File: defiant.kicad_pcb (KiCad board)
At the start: 2 copper layers, 126.6 x 99.2 mm, 55 parts, among them J1 Conn_01x02_Pin, SW1 SW_Push, SW2 SW_Push, SW3 SW_DP3T, T0 SW_PUSH, T1 SW_PUSH, T2 SW_PUSH, T3 SW_PUSH, T4 SW_PUSH, U1 Seeed Studio XIAO BLE

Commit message: Update production files
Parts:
- moved SW3 0.25 mm to (201.3, 93.6)
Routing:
- net Net-(J1-Pin_1): track 52.7 -> 34.8 mm
- net col3: track 151.6 -> 148.3 mm
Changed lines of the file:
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@@
         (effects (font (size 0.6096 0.6096) (thickness 0.0762)) (justify mirror))
     )
-    (fp_text user "XIAO" (at 0 6.5 -90 unlocked) (layer "F.SilkS")
+    (fp_text user "Seeed Studio" (at 0 4.5 -90 unlocked) (layer "F.SilkS")
         (effects (font (size 1 1) (thickness 0.15)))
     )
-    (fp_text user "Seeed Studio" (at 0 4.5 -90 unlocked) (layer "F.SilkS")
+    (fp_text user "XIAO" (at 0 6.5 -90 unlocked) (layer "F.SilkS")
         (effects (font (size 1 1) (thickness 0.15)))
     )
@@
     (pad "11" smd rect (at 9.25 0 270) (size 3 2) (layers "B.Cu" "B.Paste" "B.Mask")
       (net 24 "row3") (pinfunction "PA6_A10_D10_MOSI") (pintype "unspecified"))
+    (pad "17" thru_hole circle (at -1.27 -8.39) (size 2.2 2.2) (drill 1.5) (layers "*.Cu" "*.Mask"))
+    (pad "18" thru_hole circle (at 1.27 -8.39) (size 2.2 2.2) (drill 1.5) (layers "*.Cu" "*.Mask"))
     (pad "19" thru_hole circle (at -1.27 -5.85) (size 2.2 2.2) (drill 1.5) (layers "*.Cu" "*.Mask")
       (net 35 "Net-(U1-RESET)") (pinfunction "RESET") (pintype "input"))
@@
   )
   (footprint "Button_Switch_THT:SW_CuK_JS202011AQN_DPDT_Angled" (layer "B.Cu")
-    (at 201.277964 93.85677 -90)
+    (at 201.27 93.61 -90)
     (descr "CuK sub miniature slide switch, JS series, DPDT, right angle, http://www.ckswitches.com/media/1422/js.pdf")
     (tags "switch DPDT")
@@
   (via (at 119.176007 98.57) (size 0.8) (drill 0.4) (layers "F.Cu" "B.Cu") (net 12))
   (segment (start 119.117785 100.857218) (end 119.117785 98.628222) (width 0.4) (layer "B.Cu") (net 12))
+  (segment (start 199.02 114.285891) (end 199.02 109.205505) (width 0.4) (layer "F.Cu") (net 13))
   (segment (start 163.265036 129.579225) (end 163.886009 127.961535) (width 0.4) (layer "F.Cu") (net 13))
   (segment (start 161.573594 128.929942) (end 163.265036 129.579225) (width 0.4) (layer "F.Cu") (net 13))
   (segment (start 154.24 64.88) (end 154.24 67.047218) (width 0.4) (layer "F.Cu") (net 13))
-  (segment (start 202.424109 117.69) (end 203.87 116.244109) (width 0.4) (layer "F.Cu") (net 13))
   (segment (start 154.22 83.45) (end 154.22 85.617218) (width 0.4) (layer "F.Cu") (net 13))
-  (segment (start 200.32 117.69) (end 202.424109 117.69) (width 0.4) (layer "F.Cu") (net 13))
-  (segment (start 203.87 107.416079) (end 200.100411 103.64649) (width 0.4) (layer "F.Cu") (net 13))
+  (segment (start 200.31 117.68) (end 200.31 115.575891) (width 0.4) (layer "F.Cu") (net 13))
+  (segment (start 200.100411 108.125094) (end 200.100412 102.905094) (width 0.4) (layer "F.Cu") (net 13))
+  (segment (start 200.32 117.69) (end 200.31 117.68) (width 0.4) (layer "F.Cu") (net 13))
+  (segment (start 199.02 109.205505) (end 200.100411 108.125094) (width 0.4) (layer "F.Cu") (net 13))
   (segment (start 154.12 103.11) (end 154.12 105.277218) (width 0.4) (layer "F.Cu") (net 13))
-  (segment (start 200.100411 103.64649) (end 200.100412 102.905094) (width 0.4) (layer "F.Cu") (net 13))
-  (segment (start 203.87 116.244109) (end 203.87 107.416079) (width 0.4) (layer "F.Cu") (net 13))
+  (segment (start 200.31 115.575891) (end 199.02 114.285891) (width 0.4) (layer "F.Cu") (net 13))
   (via (at 161.573594 128.929942) (size 0.8) (drill 0.4) (layers "F.Cu" "B.Cu") (net 13))
   (via (at 154.12 103.11) (size 0.8) (drill 0.4) (layers "F.Cu" "B.Cu") (net 13))
@@
   (segment (start 173.17 103) (end 173.17 105.167218) (width 0.4) (layer "F.Cu") (net 17))
   (segment (start 184.23 109.59) (end 173.277964 109.59) (width 0.4) (layer "F.Cu") (net 17))
-  (segment (start 202.69 118.91) (end 202.7 118.91) (width 0.4) (layer "F.Cu") (net 17))
   (segment (start 182.121227 133.808775) (end 185.330002 130.6) (width 0.4) (layer "F.Cu") (net 17))
+  (segment (start 204.98 107.08) (end 202.640411 104.740411) (width 0.4) (layer "F.Cu") (net 17))
   (segment (start 193.55 118.91) (end 184.23 109.59) (width 0.4) (layer "F.Cu") (net 17))
   (segment (start 173.251778 67.457217) (end 173.48 67.685439) (width 0.4) (layer "F.Cu") (net 17))
-  (segment (start 202.7 118.91) (end 204.72 116.89) (width 0.4) (layer "F.Cu") (net 17))
-  (segment (start 202.640411 104.740411) (end 202.640411 102.905094) (width 0.4) (layer "F.Cu") (net 17))
   (segment (start 173.48 67.685439) (end 173.48 70.95) (width 0.4) (layer "F.Cu") (net 17))
-  (segment (start 204.72 116.89) (end 204.72 106.82) (width 0.4) (layer "F.Cu") (net 17))
   (segment (start 173.277964 109.59) (end 173.277964 105.483402) (width 0.4) (layer "F.Cu") (net 17))
+  (segment (start 202.69 118.91) (end 202.7 118.91) (width 0.4) (layer "F.Cu") (net 17))
   (segment (start 173.16 83.94) (end 173.16 86.107218) (width 0.4) (layer "F.Cu") (net 17))
   (segment (start 179.554244 135.772588) (end 181.001195 136.862942) (width 0.4) (layer "F.Cu") (net 17))
-  (segment (start 204.72 106.82) (end 202.640411 104.740411) (width 0.4) (layer "F.Cu") (net 17))
+  (segment (start 202.7 118.91) (end 204.98 116.63) (width 0.4) (layer "F.Cu") (net 17))
   (segment (start 183.034784 135.614335) (end 183.034784 134.199948) (width 0.4) (layer "F.Cu") (net 17))
   (segment (start 191.925596 130.6) (end 193.845596 128.68) (width 0.4) (layer "F.Cu") (net 17))
@@
   (segment (start 202.69 118.91) (end 193.55 118.91) (width 0.4) (layer "F.Cu") (net 17))
   (segment (start 185.330002 130.6) (end 191.925596 130.6) (width 0.4) (layer "F.Cu") (net 17))
+  (segment (start 204.98 116.63) (end 204.98 107.08) (width 0.4) (layer "F.Cu") (net 17))
+  (segment (start 202.640411 104.740411) (end 202.640411 102.905094) (width 0.4) (layer "F.Cu") (net 17))
   (segment (start 202.69 123.18) (end 202.69 118.91) (width 0.4) (layer "F.Cu") (net 17))
   (segment (start 181.001195 136.862942) (end 182.044009 135.479084) (width 0.4) (layer "F.Cu") (net 17))
@@
   (segment (start 190.451784 77.890093) (end 190.451784 80.38) (width 0.4) (layer "B.Cu") (net 31))
   (segment (start 197.370412 107.405094) (end 197.370411 116.405092) (width 0.4) (layer "F.Cu") (net 32))
-  (segment (start 197.677963 91.126769) (end 196.877963 91.12677) (width 0.4) (layer "B.Cu") (net 32))
+  (segment (start 197.677963 91.126769) (end 197.68 91.128806) (width 0.4) (layer "B.Cu") (net 32))
   (segment (start 197.677963 91.126769) (end 197.677963 88.40677) (width 0.4) (layer "B.Cu") (net 32))
-  (segment (start 196.877963 91.12677) (end 196.877963 102.317963) (width 0.4) (layer "B.Cu") (net 32))
-  (segment (start 202.93 116.405093) (end 197.220412 116.405093) (width 0.4) (layer "B.Cu") (net 32))
-  (segment (start 202.93 108.37) (end 202.93 116.405093) (width 0.4) (layer "B.Cu") (net 32))
+  (segment (start 197.68 107.145505) (end 197.420412 107.405093) (width 0.4) (layer "B.Cu") (net 32))
+  (segment (start 197.68 91.128806) (end 197.68 107.145505) (width 0.4) (layer "B.Cu") (net 32))
   (segment (start 197.677963 91.126769) (end 201.677964 91.12677) (width 0.4) (layer "B.Cu") (net 32))
-  (segment (start 196.877963 102.317963) (end 202.93 108.37) (width 0.4) (layer "B.Cu") (net 32))
   (segment (start 201.677964 91.12677) (end 201.677963 88.40677) (width 0.4) (layer "B.Cu") (net 32))
-  (segment (start 199.677962 93.80677) (end 199.677963 88.406771) (width 0.4) (layer "F.Cu") (net 33))
-  (segment (start 201.127963 93.80677) (end 199.677962 93.80677) (width 0.4) (layer "F.Cu") (net 33))
+  (segment (start 199.677963 93.56) (end 201.119999 93.56) (width 0.4) (layer "F.Cu") (net 33))
+  (segment (start 199.677963 88.406771) (end 199.677963 93.56) (width 0.4) (layer "F.Cu") (net 33))
   (segment (start 201.277963 93.95677) (end 201.127963 93.80677) (width 0.4) (layer "F.Cu") (net 33))
   (segment (start 192.177963 96.731771) (end 192.177963 89.556769) (width 0.4) (layer "F.Cu") (net 34))
@@
   (segment (start 185.067963 107.716769) (end 182.647963 107.716769) (width 0.4) (layer "B.Cu") (net 36))
   (segment (start 185.077963 107.706769) (end 185.067963 107.716769) (width 0.4) (layer "B.Cu") (net 36))
-  (segment (start 196.877963 104.947542) (end 196.877963 98.80677) (width 0.4) (layer "F.Cu") (net 38))
   (segment (start 195.071249 108.461408) (end 195.195411 108.428131) (width 0.4) (layer "F.Cu") (net 38))
-  (segment (start 195.320412 106.505093) (end 196.877963 104.947542) (width 0.4) (layer "F.Cu") (net 38))
   (segment (start 201.127962 98.80677) (end 201.277963 98.95677) (width 0.4) (layer "F.Cu") (net 38))
   (segment (start 195.195412 111.55677) (end 195.195411 116.405092) (width 0.4) (layer "F.Cu") (net 38))
@@
   (segment (start 195.195412 107.405094) (end 195.195412 107.95677) (width 0.4) (layer "F.Cu") (net 38))
   (segment (start 195.320412 107.405093) (end 195.320412 106.505093) (width 0.4) (layer "F.Cu") (net 38))
-  (segment (start 196.877963 98.80677) (end 201.127962 98.80677) (width 0.4) (layer "F.Cu") (net 38))
   (segment (start 195.195413 110.05677) (end 195.195412 111.55677) (width 0.4) (layer "F.Cu") (net 38))
+  (segment (start 196.877963 104.947542) (end 196.877963 98.567964) (width 0.4) (layer "F.Cu") (net 38))
+  (segment (start 196.885927 98.56) (end 201.119998 98.56) (width 0.4) (layer "F.Cu") (net 38))
+  (segment (start 195.320412 106.505093) (end 196.877963 104.947542) (width 0.4) (layer "F.Cu") (net 38))
+  (segment (start 196.877963 98.567964) (end 196.885927 98.56) (width 0.4) (layer "F.Cu") (net 38))
   (group "" (id f99f9b6d-dce2-49aa-afe9-8a8fe0581adc)
     (members

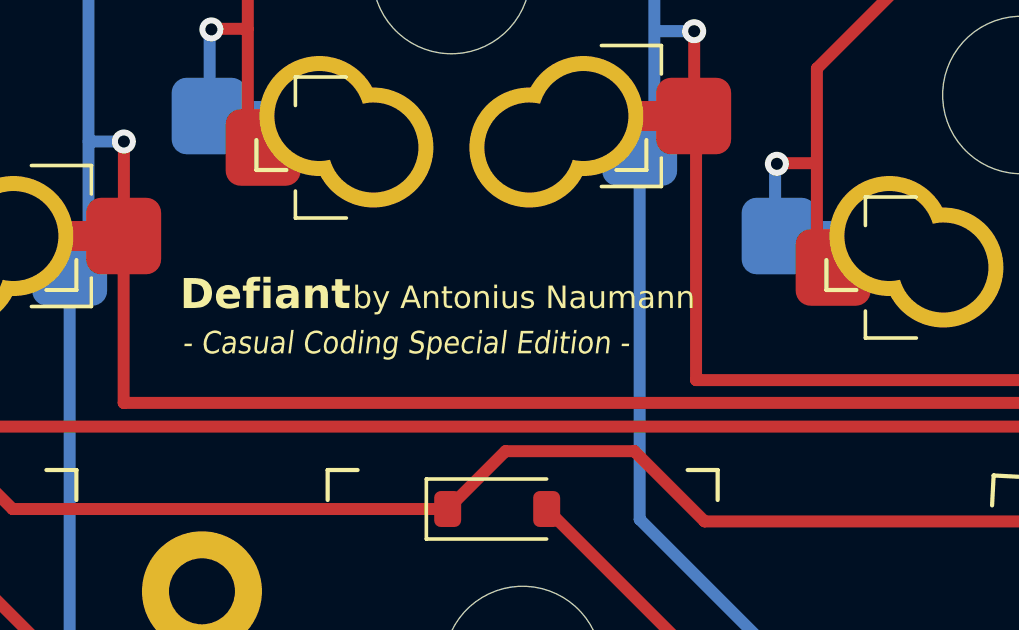
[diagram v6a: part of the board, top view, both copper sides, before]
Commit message: Update silk screen
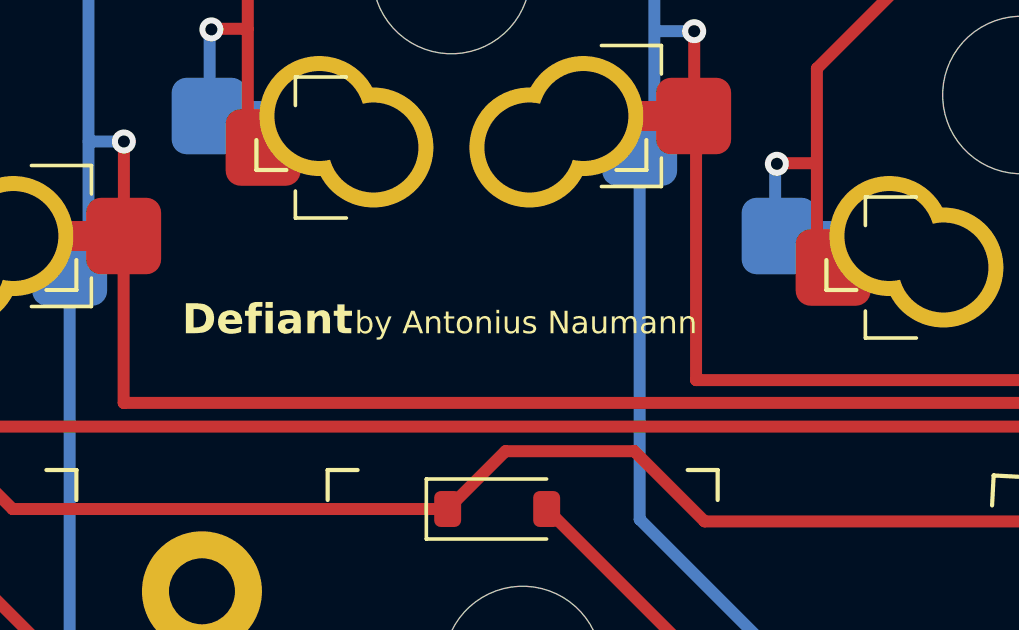
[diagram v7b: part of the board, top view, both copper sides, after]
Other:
- board text removed: "- Casual Coding Special Edition -"
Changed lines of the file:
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@@
     )
     (stroke (width 0.15) (type default)) (fill none) (layer "User.9"))
-  (gr_text "Defiant\n" (at 136.26 107.99) (layer "B.SilkS")
+  (gr_text "Defiant\n" (at 136.33 108.83) (layer "B.SilkS")
     (effects (font (size 1 1) (thickness 0.2) bold) (justify left bottom mirror))
   )
-  (gr_text "by Antonius Naumann" (at 130.51 107.96) (layer "B.SilkS")
+  (gr_text "by Antonius Naumann" (at 130.58 108.8) (layer "B.SilkS")
     (effects (font (size 0.75 0.75) (thickness 0.15)) (justify left bottom mirror))
-  )
-  (gr_text "- Casual Coding Special Edition -" (at 136.19 109.47) (layer "B.SilkS")
-    (effects (font (size 0.75 0.67) (thickness 0.15) italic) (justify left bottom mirror))
   )
   (gr_text "JLCJLCJLCJLC" (at 159.727963 93.50677) (layer "F.SilkS")
     (effects (font (size 1 1) (thickness 0.15)) (justify left bottom))
   )
-  (gr_text "by Antonius Naumann" (at 123.88 107.95) (layer "F.SilkS")
+  (gr_text "by Antonius Naumann" (at 123.95 108.79) (layer "F.SilkS")
     (effects (font (size 0.75 0.75) (thickness 0.15)) (justify left bottom))
   )
-  (gr_text "- Casual Coding Special Edition -" (at 118.2 109.46) (layer "F.SilkS")
-    (effects (font (size 0.75 0.67) (thickness 0.15) italic) (justify left bottom))
-  )
-  (gr_text "Defiant\n" (at 118.13 107.98) (layer "F.SilkS")
+  (gr_text "Defiant\n" (at 118.2 108.82) (layer "F.SilkS")
     (effects (font (size 1 1) (thickness 0.2) bold) (justify left bottom))
   )

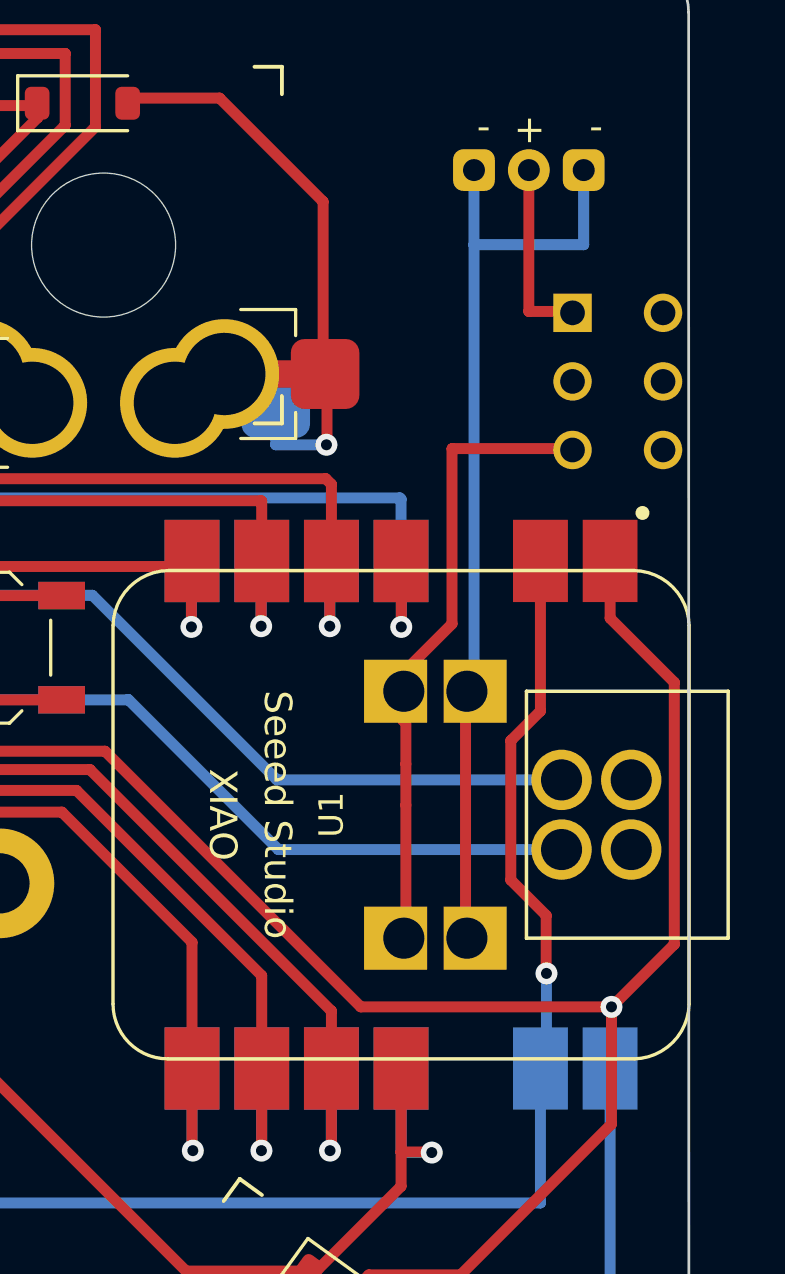
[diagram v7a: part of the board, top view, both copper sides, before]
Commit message: Fix power switch wiring
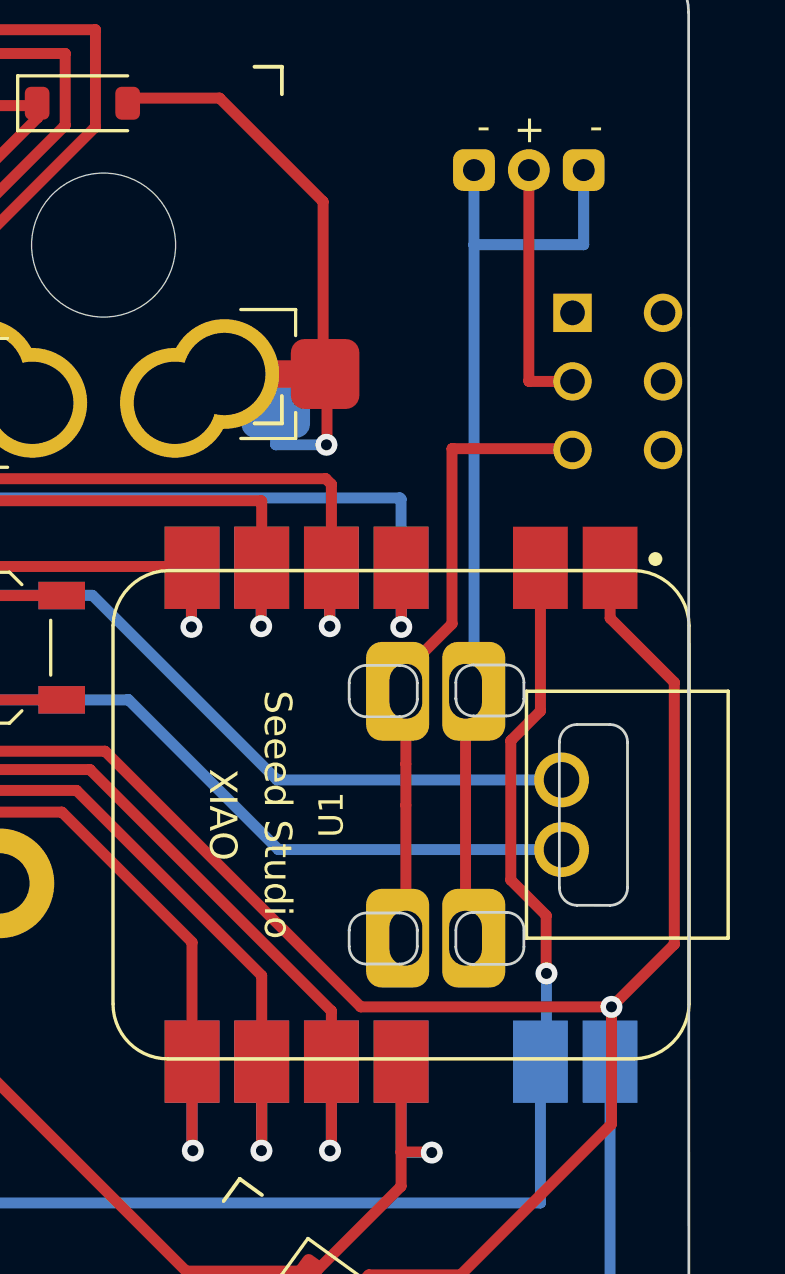
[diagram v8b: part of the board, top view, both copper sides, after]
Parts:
- U1: footprint Seeedstudio XIAO:XIAO-nRF52840-Sense-14P-2.54-21X17.8MM_Reduced_Pins -> Seeedstudio XIAO:XIAO-nRF52840-Sense-14P-2.54-21X17.8MM_NoLED_Handsolder
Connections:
- SW3 pad 1: Net-(J1-Pin_2) -> unconnected-(SW3-Pad1)
- SW3 pad 2: unconnected-(SW3-Pad2) -> Net-(J1-Pin_2)
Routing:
- net Net-(J1-Pin_2): track 6.81 -> 9.29 mm
